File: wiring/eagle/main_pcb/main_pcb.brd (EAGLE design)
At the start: 100.1 x 79.8 mm, 19 parts

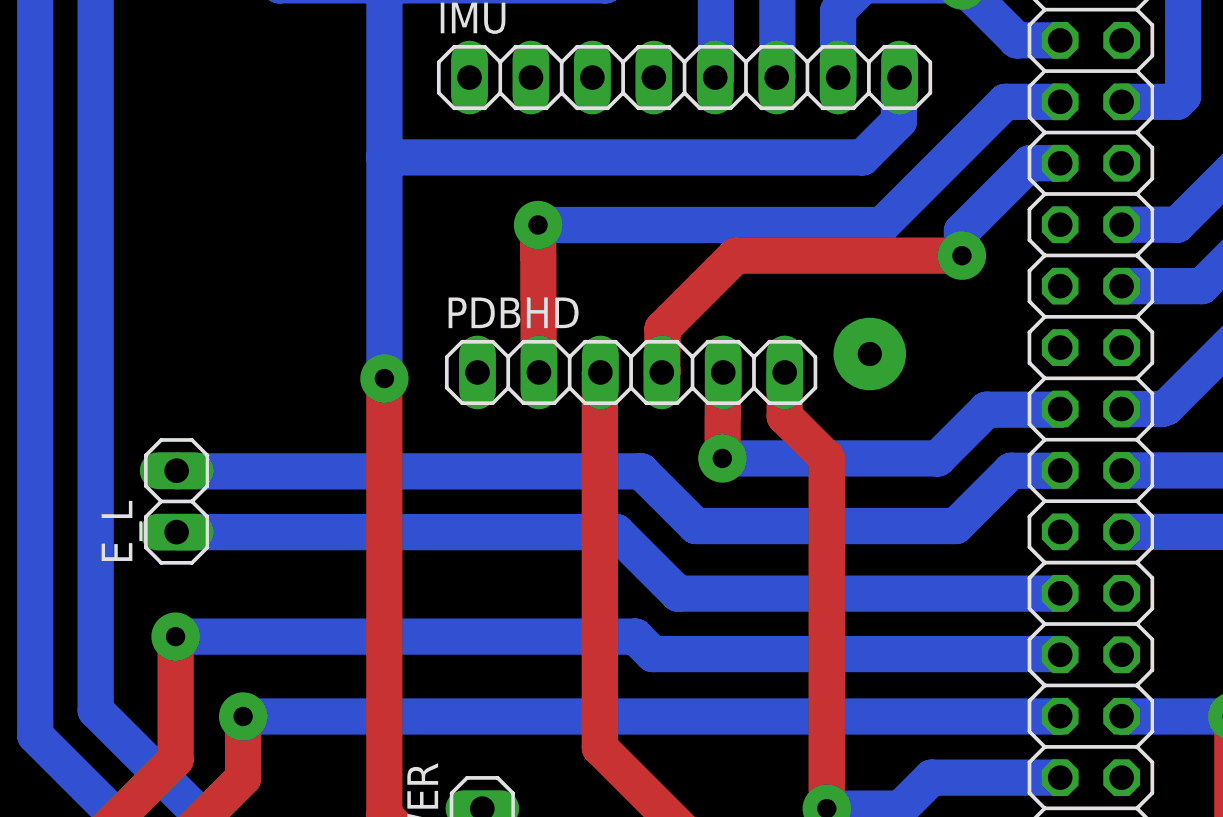
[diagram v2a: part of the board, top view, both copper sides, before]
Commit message: Encoders, roomba, PID (#29)
* Started drive control software node, need to integrate with ros and write encoder reading software

* changed us data type

* Change package structure

* Fix typo in deploy.sh

* Added Roomba control node. This mostly works, but crues/motors.py does nothing, for reasons totally beyond us.

* The rooba roombas!

* Add roomba script which does the samething without involving ROS.

* Refactor ultrasonic module, and add code for getting scan of all three ranges

* Add timeout to get_range() - cf. #13

* Move GPIO configuration to a dedicated function, so that it is run only once.

* Handle UltrasonicTimeout in ROS node.

* Increased ultrasonic timeout based on HC-SR04 datasheet.

* Update deploy script paths

* Move launch file - 'robot' is already a ROS package, apparently.

* Better logging

* Change pin definitions to ones used on PCB (may need to be double checked)

* Add an LED module.

Only problem is interrupting flashing LED relies on Event stored in state, so any ROS nodes calling this must be using the same Python process. I think.

* Support multiple ultrasonic sensors.

* Better roomba node

* Add ROS LED node and make roomba turn lights on and off.

* Add eagle files

* Add PDFs

* Load pin numbers from JSON config file.

* Fixed a few issues with the roomba code. Still doesn't work consistently.

* Increase insulation around spacer holes to 5mm

* Add IMU spacer and other minor adjustments

* Add files via upload

* Add IP address config file

* Make deploy script talk to you.

* Fix roomba code

* Fix LED node (swapped green and red LEDs - green is now on the outside)

* Add encoder node

* Make changes to PCB to avoid using pin 27

* Wrong pins in new config file

* Make encoder node parameterised

* Parameterise LEDs

* Separate out drive nodes and rename launch file to roomba.launch

* Use Twist message to communicate with differential-drive packag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
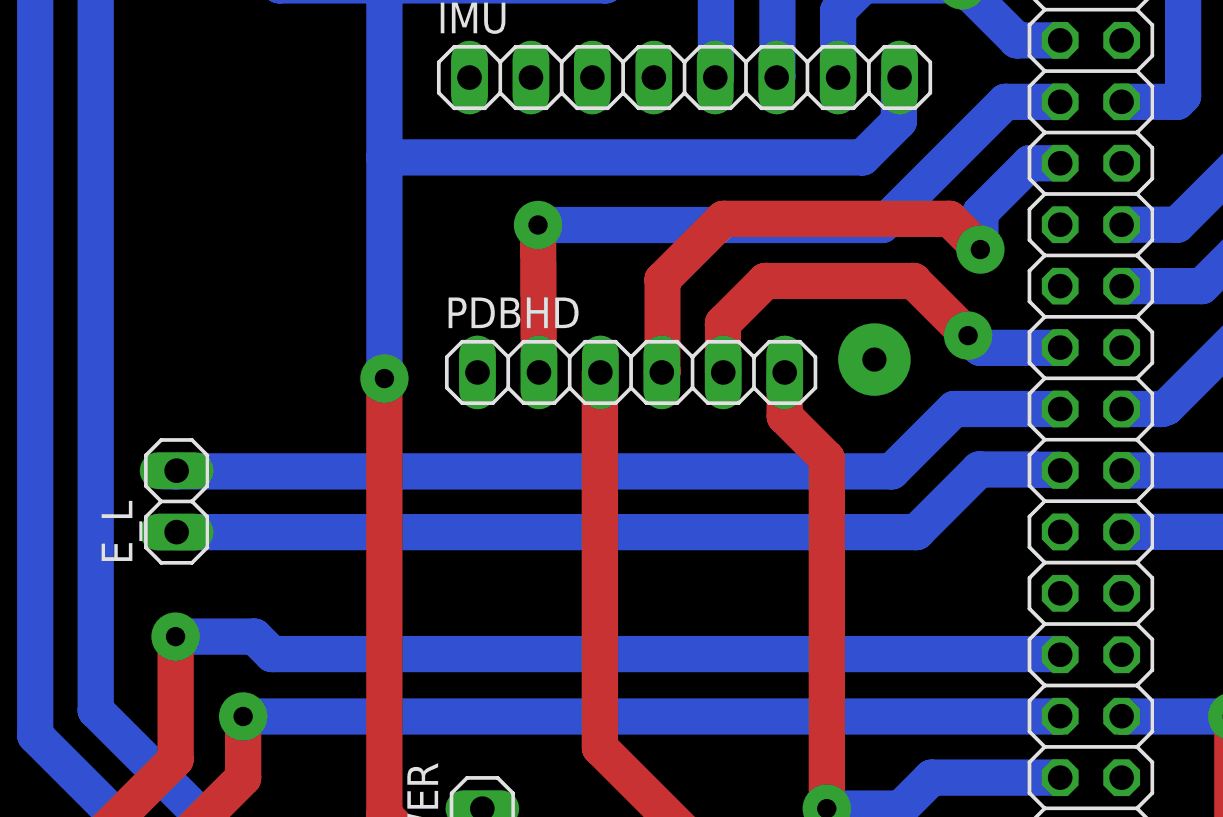
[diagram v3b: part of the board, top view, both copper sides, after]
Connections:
- removed net EL_A: E_L.2, PIHD.23
- removed net EL_B: E_L.1, PIHD.27
- new net N$1: E_L.2, PIHD.21
- new net N$2: E_L.1, PIHD.23
- net RDIR: now also PIHD.19; no longer PIHD.21
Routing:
- net EL_A: track 38.4 -> 0.00 mm
- net N$1: track 0.00 -> 38.2 mm
- net N$2: track 0.00 -> 37.6 mm
- net EL_B: track 37.6 -> 0.00 mm
- net SLP: track 21.9 -> 24.2 mm
- net RDIR: track 18.4 -> 17.9 mm
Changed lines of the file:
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@@
 <param name="mdDrill" value="0.8mm"/>
 <param name="mdSmdStop" value="0mil"/>
-<param name="msWidth" value="0.6mm"/>
-<param name="msDrill" value="0.1mm"/>
+<param name="msWidth" value="1.5mm"/>
+<param name="msDrill" value="0.8mm"/>
 <param name="msMicroVia" value="9.99mm"/>
 <param name="msBlindViaRatio" value="0.5"/>
@@
 <contactref element="PDBHD" pad="4"/>
 <contactref element="PIHD" pad="13"/>
-<wire x1="49.088" y1="33.04450625" x2="49.088" y2="31.27" width="1.5" layer="1"/>
+<wire x1="49.088" y1="35.07650625" x2="49.088" y2="31.27" width="1.5" layer="1"/>
 <wire x1="49.088" y1="31.27" x2="49.06" y2="31.242" width="1.5" layer="1"/>
-<wire x1="61.468" y1="36.068" x2="52.11149375" y2="36.068" width="1.5" layer="1"/>
-<wire x1="52.11149375" y1="36.068" x2="49.088" y2="33.04450625" width="1.5" layer="1"/>
-<wire x1="65.53" y1="39.89" x2="65.29" y2="39.89" width="1.5" layer="16"/>
-<via x="61.468" y="36.068" extent="1-16" drill="0.8" diameter="2"/>
+<wire x1="62.23" y1="36.322" x2="60.96" y2="37.592" width="1.5" layer="1"/>
+<wire x1="60.96" y1="37.592" x2="51.60349375" y2="37.592" width="1.5" layer="1"/>
+<wire x1="51.60349375" y1="37.592" x2="49.088" y2="35.07650625" width="1.5" layer="1"/>
+<via x="62.23" y="36.322" extent="1-16" drill="0.8" diameter="2"/>
+<wire x1="64.274" y1="39.89" x2="62.23" y2="37.846" width="1.5" layer="16"/>
+<wire x1="62.23" y1="37.846" x2="62.23" y2="36.322" width="1.5" layer="16"/>
 <wire x1="65.53" y1="39.89" x2="64.274" y2="39.89" width="1.5" layer="16"/>
-<wire x1="64.274" y1="39.89" x2="61.468" y2="37.084" width="1.5" layer="16"/>
-<wire x1="61.468" y1="37.084" x2="61.468" y2="36.068" width="1.5" layer="16"/>
 </signal>
 <signal name="RDIR">
 <contactref element="PDBHD" pad="5"/>
-<via x="51.562" y="27.686" extent="1-16" drill="0.8" diameter="2"/>
-<wire x1="51.562" y1="27.686" x2="51.6" y2="31.242" width="1.5" layer="1"/>
-<contactref element="PIHD" pad="21"/>
-<wire x1="65.502" y1="29.702" x2="65.53" y2="29.73" width="1.5" layer="16"/>
-<wire x1="60.4724625" y1="27.686" x2="62.4884625" y2="29.702" width="1.5" layer="16"/>
-<wire x1="62.4884625" y1="29.702" x2="65.502" y2="29.702" width="1.5" layer="16"/>
-<wire x1="51.562" y1="27.686" x2="60.4724625" y2="27.686" width="1.5" layer="16"/>
+<contactref element="PIHD" pad="19"/>
+<wire x1="51.6" y1="31.242" x2="51.588" y2="31.254" width="1.5" layer="1"/>
+<wire x1="51.588" y1="31.254" x2="51.588" y2="33.274" width="1.5" layer="1"/>
+<wire x1="51.588" y1="33.274" x2="53.338" y2="35.024" width="1.5" layer="1"/>
+<wire x1="53.338" y1="35.024" x2="59.464" y2="35.024" width="1.5" layer="1"/>
+<wire x1="59.464" y1="35.024" x2="61.722" y2="32.766" width="1.5" layer="1"/>
+<via x="61.722" y="32.766" extent="1-16" drill="0.8" diameter="2"/>
+<wire x1="65.518" y1="32.258" x2="62.23" y2="32.258" width="1.5" layer="16"/>
+<wire x1="62.23" y1="32.258" x2="61.722" y2="32.766" width="1.5" layer="16"/>
+<wire x1="65.53" y1="32.27" x2="65.518" y2="32.258" width="1.5" layer="16"/>
 </signal>
 <signal name="LPWM">
@@
 <wire x1="21.844" y1="9.398" x2="18.034" y2="5.588" width="1.5" layer="16"/>
 <wire x1="18.034" y1="5.588" x2="15.24" y2="5.588" width="1.5" layer="16"/>
-<wire x1="28.956" y1="20.32" x2="47.9678375" y2="20.32" width="1.5" layer="16"/>
-<wire x1="47.9678375" y1="20.32" x2="48.6898375" y2="19.598" width="1.5" layer="16"/>
-<wire x1="48.6898375" y1="19.598" x2="65.502" y2="19.598" width="1.5" layer="16"/>
+<wire x1="28.956" y1="20.32" x2="32.2198375" y2="20.32" width="1.5" layer="16"/>
+<wire x1="32.2198375" y1="20.32" x2="32.9418375" y2="19.598" width="1.5" layer="16"/>
+<wire x1="32.9418375" y1="19.598" x2="65.502" y2="19.598" width="1.5" layer="16"/>
 <wire x1="65.502" y1="19.598" x2="65.53" y2="19.57" width="1.5" layer="16"/>
 <wire x1="28.956" y1="15.24" x2="28.956" y2="20.32" width="1.5" layer="1"/>
@@
 <wire x1="70.37" y1="37.35" x2="73.152" y2="40.132" width="1.5" layer="16"/>
 </signal>
-<signal name="EL_A">
-<contactref element="E_L" pad="2"/>
-<contactref element="PIHD" pad="23"/>
-<wire x1="50.4669125" y1="24.892" x2="61.214" y2="24.892" width="1.5" layer="16"/>
-<wire x1="61.214" y1="24.892" x2="63.5" y2="27.178" width="1.5" layer="16"/>
-<wire x1="63.5" y1="27.178" x2="65.518" y2="27.178" width="1.5" layer="16"/>
-<wire x1="65.518" y1="27.178" x2="65.53" y2="27.19" width="1.5" layer="16"/>
-<wire x1="29" y1="27.18" x2="29.028" y2="27.152" width="1.5" layer="16"/>
-<wire x1="29.028" y1="27.152" x2="48.2069125" y2="27.152" width="1.5" layer="16"/>
-<wire x1="48.2069125" y1="27.152" x2="50.4669125" y2="24.892" width="1.5" layer="16"/>
-</signal>
-<signal name="EL_B">
-<contactref element="E_L" pad="1"/>
-<contactref element="PIHD" pad="27"/>
-<wire x1="65.518" y1="22.098" x2="65.53" y2="22.11" width="1.5" layer="16"/>
-<wire x1="65.518" y1="22.098" x2="49.725375" y2="22.098" width="1.5" layer="16"/>
-<wire x1="47.183375" y1="24.64" x2="29" y2="24.64" width="1.5" layer="16"/>
-<wire x1="49.725375" y1="22.098" x2="47.183375" y2="24.64" width="1.5" layer="16"/>
-</signal>
 <signal name="ER_A">
 <contactref element="E_R" pad="1"/>
@@
 </signal>
 <signal name="SPACER_IMU">
-<via x="57.658" y="32.004" extent="1-16" drill="1" diameter="3"/>
+<via x="57.85" y="31.774" extent="1-16" drill="1" diameter="3"/>
+</signal>
+<signal name="N$1">
+<contactref element="E_L" pad="2"/>
+<contactref element="PIHD" pad="21"/>
+<wire x1="65.53" y1="29.73" x2="61.1437375" y2="29.73" width="1.5" layer="16"/>
+<wire x1="61.1437375" y1="29.73" x2="58.5657375" y2="27.152" width="1.5" layer="16"/>
+<wire x1="58.5657375" y1="27.152" x2="28.972" y2="27.152" width="1.5" layer="16"/>
+<wire x1="28.448" y1="27.152" x2="28.972" y2="27.152" width="1.5" layer="16"/>
+<wire x1="28.972" y1="27.152" x2="29" y2="27.18" width="1.5" layer="16"/>
+</signal>
+<signal name="N$2">
+<contactref element="E_L" pad="1"/>
+<contactref element="PIHD" pad="23"/>
+<wire x1="29" y1="24.64" x2="59.589275" y2="24.64" width="1.5" layer="16"/>
+<wire x1="59.589275" y1="24.64" x2="62.179275" y2="27.23" width="1.5" layer="16"/>
+<wire x1="62.179275" y1="27.23" x2="64.47749375" y2="27.23" width="1.5" layer="16"/>
+<wire x1="64.47749375" y1="27.23" x2="64.48949375" y2="27.218" width="1.5" layer="16"/>
+<wire x1="64.48949375" y1="27.218" x2="65.502" y2="27.218" width="1.5" layer="16"/>
+<wire x1="65.502" y1="27.218" x2="65.53" y2="27.19" width="1.5" layer="16"/>
 </signal>
 </signals>
